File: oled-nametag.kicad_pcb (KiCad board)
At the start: 4 copper layers, 88 x 30 mm, 119 parts, among them J1 USB_C_Receptacle_USB2.0, J2 I2C, Q1 AO3401A, Q2 AO3401A, Q3 FS8205A, Q6 2N7002, SW1 Power, SW2 BTN1, SW3 BTN2, SW4 BTN3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

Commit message: Start rev1.1
Fixed bugs:
 - Swapped D+ and D-
 - Insufficient pull-down strength on VBUS
 - Default OLED to 4-wire SPI
 - Swap VBUS detect divider from 2/3 to 1/3
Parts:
- R21: value 47k -> 1k
- R28: value 5.1k -> 10k
- R30: value 10k -> 5.1k
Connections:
- R1 pad 1: +3V3 -> GND
- U3 pad 25: /ESP32/D+ -> /ESP32/D-
- U3 pad 26: /ESP32/D- -> /ESP32/D+
- U9 pad 4: /ESP32/D- -> /ESP32/D+
- U9 pad 6: /ESP32/D+ -> /ESP32/D-
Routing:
- net +3V3: track 67.1 -> 57.3 mm, vias 23 -> 22
- net GND: track 161.5 -> 163.5 mm
- net /ESP32/D-: track 52.1 -> 50.8 mm
- net /ESP32/D+: track 50.6 -> 51.2 mm
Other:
- board text added: "OLED Badge Rev 1.1 2023"
- board text removed: "OLED Badge Rev 1.0 2023"

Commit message: More Rev 1.1 fixes
- Revert USB_DET voltage divider swap
- Fix battery gauge temperature sensor reference level
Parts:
- R28: value 10k -> 5.1k
- R30: value 5.1k -> 10k
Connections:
- R33 pad 2: GND1 -> Net-(U10-VCC)
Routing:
- net Net-(U10-VCC): track 1.30 -> 5.02 mm, vias 0 -> 2
- net GND1: track 16.0 -> 15.4 mm, vias 20 -> 19
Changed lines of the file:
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@@
       (net 92 "Net-(U10-TS)") (pintype "passive"))
     (pad "2" smd roundrect (at 0.51 0) (size 0.54 0.64) (layers "F.Cu" "F.Paste" "F.Mask") (roundrect_rratio 0.25)
-      (net 16 "GND1") (pintype "passive"))
+      (net 17 "Net-(U10-VCC)") (pintype "passive"))
     (model "${KICAD6_3DMODEL_DIR}/Resistor_SMD.3dshapes/R_0402_1005Metric.wrl"
       (offset (xyz 0 0 0))
@@
     (descr "Resistor SMD 0402 (1005 Metric), square (rectangular) end terminal, IPC_7351 nominal, (Body size source: IPC-SM-782 page 72, https://www.pcb-3d.com/wordpress/wp-content/uploads/ipc-sm-782a_amendment_1_and_2.pdf), generated with kicad-footprint-generator")
     (tags "resistor")
-    (property "LCSC" "C25744")
+    (property "LCSC" "C25905")
     (property "Sheetfile" "power.kicad_sch")
     (property "Sheetname" "Power")
@@
         (effects (font (size 1 1) (thickness 0.15)))
     )
-    (fp_text value "10k" (at 0 1.17 90) (layer "F.Fab")
+    (fp_text value "5.1k" (at 0 1.17 90) (layer "F.Fab")
         (effects (font (size 1 1) (thickness 0.15)))
     )
@@
     (descr "Resistor SMD 0402 (1005 Metric), square (rectangular) end terminal, IPC_7351 nominal, (Body size source: IPC-SM-782 page 72, https://www.pcb-3d.com/wordpress/wp-content/uploads/ipc-sm-782a_amendment_1_and_2.pdf), generated with kicad-footprint-generator")
     (tags "resistor")
-    (property "LCSC" "C25905")
+    (property "LCSC" "C25744")
     (property "Sheetfile" "power.kicad_sch")
     (property "Sheetname" "Power")
@@
         (effects (font (size 1 1) (thickness 0.15)))
     )
-    (fp_text value "5.1k" (at 0 1.17 90) (layer "F.Fab")
+    (fp_text value "10k" (at 0 1.17 90) (layer "F.Fab")
         (effects (font (size 1 1) (thickness 0.15)))
     )
@@
   (segment (start 87.85 36.8) (end 87.5 36.8) (width 0.127) (layer "F.Cu") (net 16))
   (segment (start 90.100001 37.2) (end 90.1 36.3) (width 0.127) (layer "F.Cu") (net 16))
-  (segment (start 88.379999 38.9) (end 88.95 38.9) (width 0.127) (layer "F.Cu") (net 16))
   (segment (start 87.5 36.8) (end 87.35 36.8) (width 0.127) (layer "F.Cu") (net 16))
   (segment (start 89.15 37.25) (end 88.95 37.05) (width 0.127) (layer "F.Cu") (net 16))
@@
   (via (at 72.35 34.05) (size 0.45) (drill 0.3) (layers "F.Cu" "B.Cu") (net 16))
   (via (at 73.55 31.55) (size 0.45) (drill 0.3) (layers "F.Cu" "B.Cu") (net 16))
-  (via (at 88.95 38.9) (size 0.45) (drill 0.3) (layers "F.Cu" "B.Cu") (net 16))
   (via (at 105.75 38.75) (size 0.45) (drill 0.3) (layers "F.Cu" "B.Cu") (net 16))
   (via (at 22.25 38.65) (size 0.45) (drill 0.3) (layers "F.Cu" "B.Cu") (net 16))
@@
   (via (at 72.05 31.55) (size 0.45) (drill 0.3) (layers "F.Cu" "B.Cu") (net 16))
   (via (at 72.8 31.55) (size 0.45) (drill 0.3) (layers "F.Cu" "B.Cu") (net 16))
-  (segment (start 89.15 36.3) (end 87.85 36.3) (width 0.127) (layer "F.Cu") (net 17))
+  (segment (start 89.15 36.3) (end 88.55 36.3) (width 0.127) (layer "F.Cu") (net 17))
+  (segment (start 88.379999 38.9) (end 88.95 38.9) (width 0.127) (layer "F.Cu") (net 17))
+  (segment (start 88.55 36.3) (end 88.55 36.15) (width 0.127) (layer "F.Cu") (net 17))
+  (segment (start 88.55 36.3) (end 87.85 36.3) (width 0.127) (layer "F.Cu") (net 17))
+  (via (at 88.55 36.15) (size 0.45) (drill 0.2) (layers "F.Cu" "B.Cu") (net 17))
+  (via (at 88.95 38.9) (size 0.45) (drill 0.2) (layers "F.Cu" "B.Cu") (net 17))
+  (segment (start 89.05 38.8) (end 88.95 38.9) (width 0.127) (layer "B.Cu") (net 17))
+  (segment (start 89.05 36.65) (end 89.05 38.8) (width 0.127) (layer "B.Cu") (net 17))
+  (segment (start 88.55 36.15) (end 89.05 36.65) (width 0.127) (layer "B.Cu") (net 17))
   (segment (start 86.320002 34.7) (end 87.12 34.7) (width 0.127) (layer "F.Cu") (net 18))
   (segment (start 87.349999 35.8) (end 87.35 34.7) (width 0.127) (layer "F.Cu") (net 18))

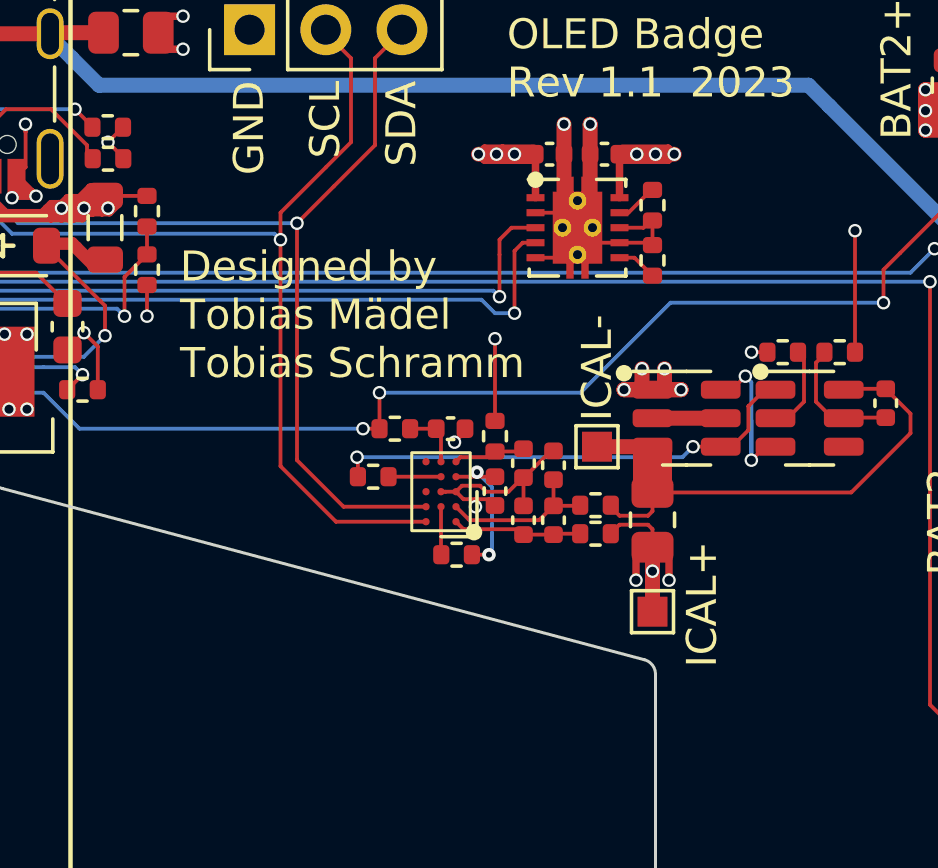
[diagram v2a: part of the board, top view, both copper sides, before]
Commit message: Reduce charge current to 300mA, Add battery voltage calibration testpoint
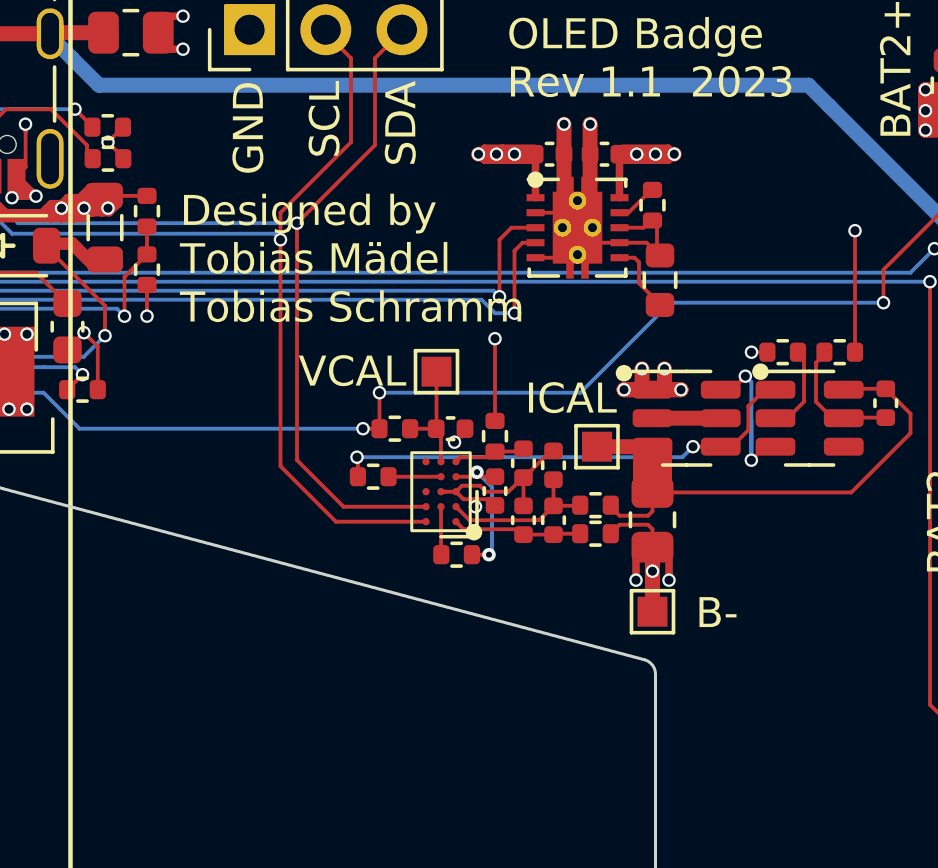
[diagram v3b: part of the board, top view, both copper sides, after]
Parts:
- added TP10: VCAL, TestPoint:TestPoint_Pad_1.0x1.0mm, F.Cu at (87.2, 32.8)
- R14: value 1k -> 2.7k; footprint Resistor_SMD:R_0402_1005Metric -> Resistor_SMD:R_0603_1608Metric
- moved R14 0.71 mm to (94.7, 29.8)
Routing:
- net Net-(U10-BAT): track 1.90 -> 3.80 mm
- net Net-(U8-ISET): track 1.35 -> 2.40 mm
- net GND: track 163.5 -> 164.4 mm
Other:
- board text added: "B-"
- board text added: "ICAL"
- board text added: "VCAL"
- board text removed: "ICAL+"
- board text removed: "ICAL-"

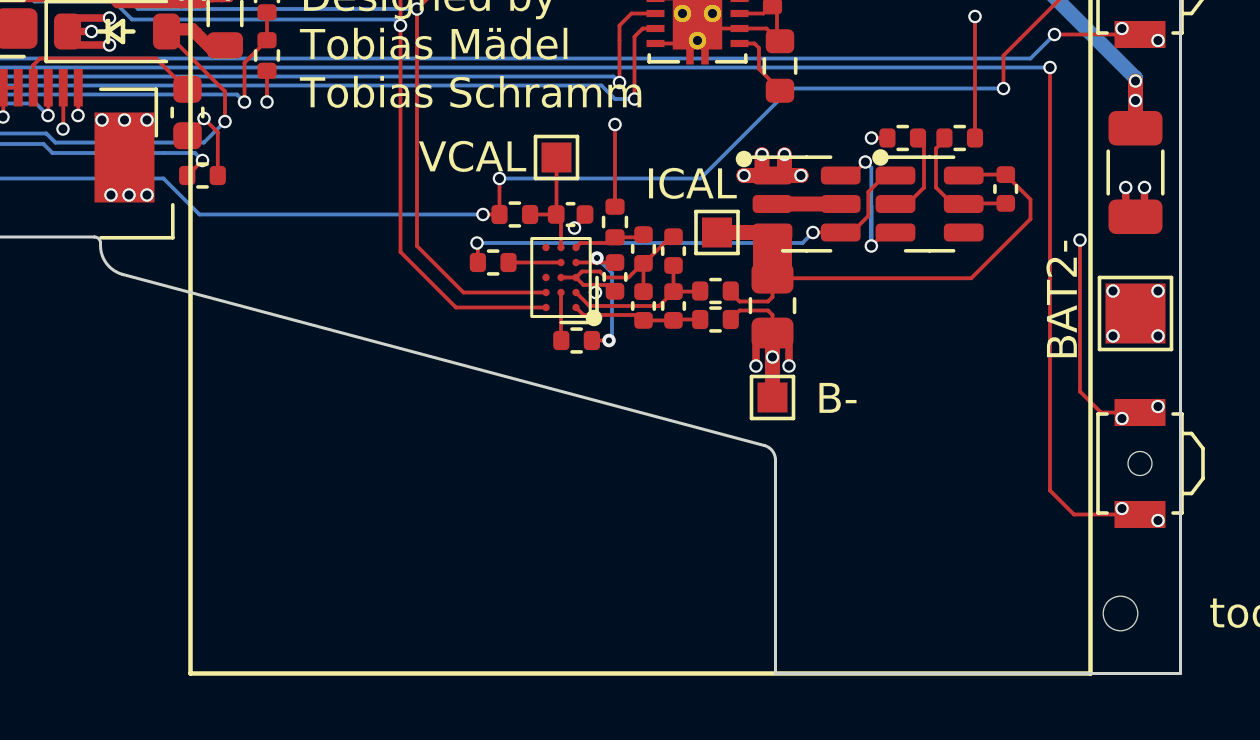
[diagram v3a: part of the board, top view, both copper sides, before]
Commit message: Add current calibration output
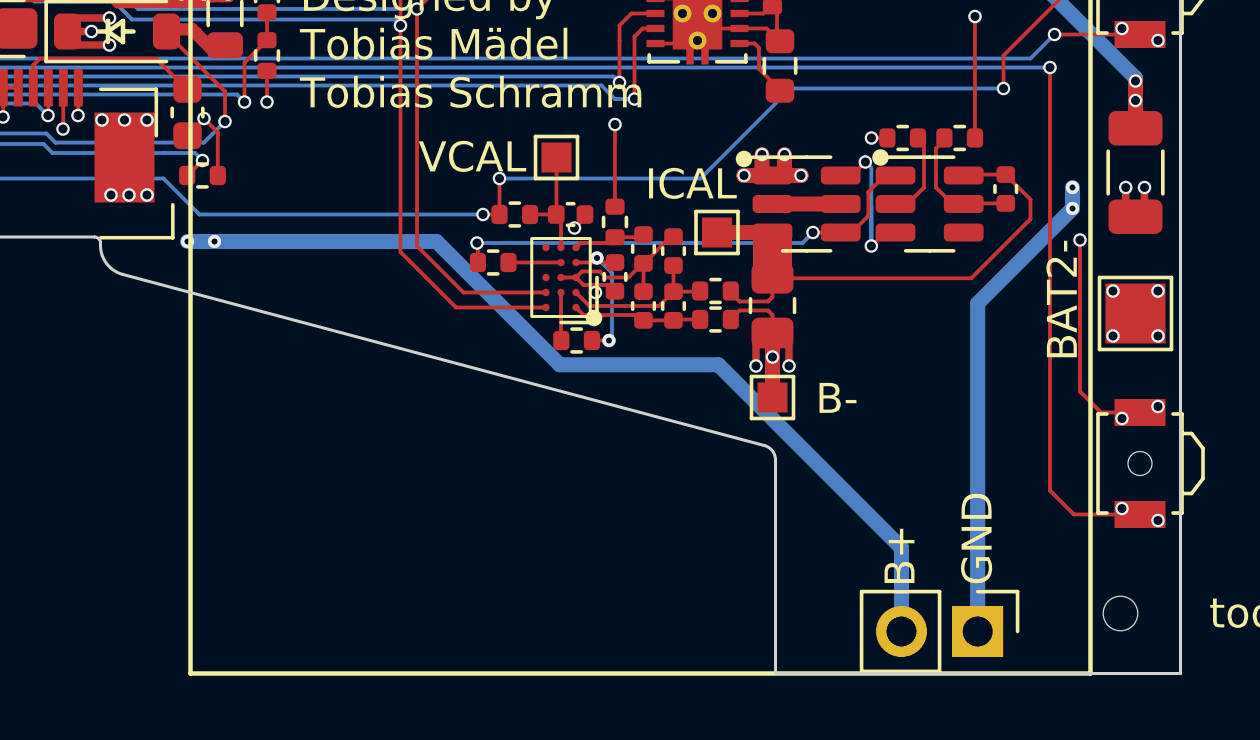
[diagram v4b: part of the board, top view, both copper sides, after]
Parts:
- added J3: LOAD, Connector_PinHeader_2.54mm:PinHeader_1x02_P2.54mm_Vertical, F.Cu at (101.2, 48.6)
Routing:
- net +BATT: track 129.4 -> 160.2 mm, vias 22 -> 24
- net GND: track 164.4 -> 180.5 mm, vias 90 -> 92
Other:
- board text added: "B+"
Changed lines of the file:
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@@
     )
   )
+  (footprint "Connector_PinHeader_2.54mm:PinHeader_1x02_P2.54mm_Vertical" (layer "F.Cu")
+    (at 101.24 48.6 -90)
+    (descr "Through hole straight pin header, 1x02, 2.54mm pitch, single row")
+    (tags "Through hole pin header THT 1x02 2.54mm single row")
+    (property "Sheetfile" "power.kicad_sch")
+    (property "Sheetname" "Power")
+    (property "ki_description" "Generic connector, single row, 01x02, script generated (kicad-library-utils/schlib/autogen/connector/)")
+    (property "ki_keywords" "connector")
+    (attr through_hole)
+    (fp_text reference "J3" (at 0 -2.33 90) (layer "F.SilkS") hide
+        (effects (font (size 1 1) (thickness 0.15)))
+    )
+    (fp_text value "LOAD" (at 0 4.87 90) (layer "F.Fab")
+        (effects (font (size 1 1) (thickness 0.15)))
+    )
+    (fp_text user "${REFERENCE}" (at 0 1.27) (layer "F.Fab")
+        (effects (font (size 1 1) (thickness 0.15)))
+    )
+    (fp_line (start -1.33 -1.33) (end 0 -1.33)
+      (stroke (width 0.12) (type solid)) (layer "F.SilkS"))
+    (fp_line (start -1.33 0) (end -1.33 -1.33)
+      (stroke (width 0.12) (type solid)) (layer "F.SilkS"))
+    (fp_line (start -1.33 1.27) (end -1.33 3.87)
+      (stroke (width 0.12) (type solid)) (layer "F.SilkS"))
+    (fp_line (start -1.33 1.27) (end 1.33 1.27)
+      (stroke (width 0.12) (type solid)) (layer "F.SilkS"))
+    (fp_line (start -1.33 3.87) (end 1.33 3.87)
+      (stroke (width 0.12) (type solid)) (layer "F.SilkS"))
+    (fp_line (start 1.33 1.27) (end 1.33 3.87)
+      (stroke (width 0.12) (type solid)) (layer "F.SilkS"))
+    (fp_line (start -1.8 -1.8) (end -1.8 4.35)
+      (stroke (width 0.05) (type solid)) (layer "F.CrtYd"))
+    (fp_line (start -1.8 4.35) (end 1.8 4.35)
+      (stroke (width 0.05) (type solid)) (layer "F.CrtYd"))
+    (fp_line (start 1.8 -1.8) (end -1.8 -1.8)
+      (stroke (width 0.05) (type solid)) (layer "F.CrtYd"))
+    (fp_line (start 1.8 4.35) (end 1.8 -1.8)
+      (stroke (width 0.05) (type solid)) (layer "F.CrtYd"))
+    (fp_line (start -1.27 -0.635) (end -0.635 -1.27)
+      (stroke (width 0.1) (type solid)) (layer "F.Fab"))
+    (fp_line (start -1.27 3.81) (end -1.27 -0.635)
+      (stroke (width 0.1) (type solid)) (layer "F.Fab"))
+    (fp_line (start -0.635 -1.27) (end 1.27 -1.27)
+      (stroke (width 0.1) (type solid)) (layer "F.Fab"))
+    (fp_line (start 1.27 -1.27) (end 1.27 3.81)
+      (stroke (width 0.1) (type solid)) (layer "F.Fab"))
+    (fp_line (start 1.27 3.81) (end -1.27 3.81)
+      (stroke (width 0.1) (type solid)) (layer "F.Fab"))
+    (pad "1" thru_hole rect (at 0 0 270) (size 1.7 1.7) (drill 1) (layers "*.Cu" "*.Mask")
+      (net 6 "GND") (pinfunction "Pin_1") (pintype "passive"))
+    (pad "2" thru_hole oval (at 0 2.54 270) (size 1.7 1.7) (drill 1) (layers "*.Cu" "*.Mask")
+      (net 15 "+BATT") (pinfunction "Pin_2") (pintype "passive"))
+  )
   (footprint "Resistor_SMD:R_0402_1005Metric" (layer "F.Cu")
     (at 44.69 27.2)
@@
   (gr_rect (start 23 20) (end 53 50)
     (stroke (width 0.15) (type solid)) (fill none) (layer "User.9"))
+  (gr_text "GND" (at 101.24 47.07 90) (layer "F.SilkS")
+    (effects (font (size 1 1) (thickness 0.15)) (justify left))
+  )
   (gr_text "GND" (at 24.55 25.4 90) (layer "F.SilkS")
     (effects (font (size 1 1) (thickness 0.15)) (justify left))
@@
     (effects (font (size 1 1) (thickness 0.15)) (justify top))
   )
+  (gr_text "B+" (at 98.67 47.12 90) (layer "F.SilkS")
+    (effects (font (size 1 1) (thickness 0.15)) (justify left))
+  )
   (gr_text "BAT2-" (at 103.5 37.55 90) (layer "F.SilkS")
     (effects (font (size 1 1) (thickness 0.15)) (justify top))
@@
   (via (at 106.175 33.8) (size 0.45) (drill 0.3) (layers "F.Cu" "B.Cu") (net 6))
   (via (at 24.55 27.65) (size 0.45) (drill 0.3) (layers "F.Cu" "B.Cu") (net 6))
+  (via (at 104.4 34.5) (size 0.45) (drill 0.2) (layers "F.Cu" "B.Cu") (net 6))
   (via (at 51.85 31.15) (size 0.45) (drill 0.3) (layers "F.Cu" "B.Cu") (net 6))
   (via (at 106.05 41.5) (size 0.45) (drill 0.3) (layers "F.Cu" "B.Cu") (net 6))
@@
   (via (at 55.25 31.55) (size 0.45) (drill 0.3) (layers "F.Cu" "B.Cu") (net 6))
   (via (at 55.340623 22.701565) (size 0.45) (drill 0.3) (layers "F.Cu" "B.Cu") (net 6))
+  (via (at 104.4 33.8) (size 0.45) (drill 0.2) (layers "F.Cu" "B.Cu") (net 6))
   (via (at 92.325 24.55) (size 0.45) (drill 0.3) (layers "F.Cu" "B.Cu") (net 6))
   (via (at 68.75 31.45) (size 0.45) (drill 0.3) (layers "F.Cu" "B.Cu") (net 6))
@@
   (via (at 49.4 29.75) (size 0.45) (drill 0.3) (layers "F.Cu" "B.Cu") (net 6))
   (via (at 106.05 25.5) (size 0.45) (drill 0.3) (layers "F.Cu" "B.Cu") (net 6))
+  (segment (start 101.24 48.6) (end 101.24 37.66) (width 0.5) (layer "B.Cu") (net 6))
+  (segment (start 104.4 34.5) (end 104.4 33.8) (width 0.5) (layer "B.Cu") (net 6))
+  (segment (start 101.24 37.66) (end 104.4 34.5) (width 0.5) (layer "B.Cu") (net 6))
   (segment (start 69.983 29.5) (end 73.85 29.5) (width 0.127) (layer "F.Cu") (net 7))
   (segment (start 69.76 30.475) (end 69.76 29.723) (width 0.127) (layer "F.Cu") (net 7))
@@
   (via (at 95.125 25.55) (size 0.45) (drill 0.3) (layers "F.Cu" "B.Cu") (net 15))
   (via (at 46.8 31.15) (size 0.45) (drill 0.3) (layers "F.Cu" "B.Cu") (net 15))
+  (via (at 74.9 35.6) (size 0.45) (drill 0.2) (layers "F.Cu" "B.Cu") (net 15))
   (via (at 85.3 33.5) (size 0.45) (drill 0.3) (layers "F.Cu" "B.Cu") (net 15))
   (via (at 45.85 31.15) (size 0.45) (drill 0.3) (layers "F.Cu" "B.Cu") (net 15))
@@
   (via (at 23.75 46.85) (size 0.45) (drill 0.3) (layers "F.Cu" "B.Cu") (net 15))
   (via (at 104.25 23.4) (size 0.45) (drill 0.3) (layers "F.Cu" "B.Cu") (net 15))
+  (via (at 75.8 35.6) (size 0.45) (drill 0.2) (layers "F.Cu" "B.Cu") (net 15))
   (via (at 93.875 25.55) (size 0.45) (drill 0.3) (layers "F.Cu" "B.Cu") (net 15))
   (via (at 22.95 46.15) (size 0.45) (drill 0.3) (layers "F.Cu" "B.Cu") (net 15))
+  (segment (start 87.31 39.71) (end 83.2 35.6) (width 0.5) (layer "B.Cu") (net 15))
   (segment (start 66.1 33.85) (end 66.45 33.5) (width 0.127) (layer "B.Cu") (net 15))
   (segment (start 95 30.5) (end 92 33.5) (width 0.127) (layer "B.Cu") (net 15))
@@
   (segment (start 102.1 30.5) (end 95 30.5) (width 0.127) (layer "B.Cu") (net 15))
   (segment (start 24.151883 41.648117) (end 24.15 41.65) (width 0.127) (layer "B.Cu") (net 15))
+  (segment (start 92.597736 39.71) (end 87.31 39.71) (width 0.5) (layer "B.Cu") (net 15))
   (segment (start 92 33.5) (end 85.3 33.5) (width 0.127) (layer "B.Cu") (net 15))
   (segment (start 53.25 34.6) (end 54 33.85) (width 0.127) (layer "B.Cu") (net 15))
+  (segment (start 98.7 45.812264) (end 92.597736 39.71) (width 0.5) (layer "B.Cu") (net 15))
   (segment (start 52.1 36.85) (end 53.25 35.7) (width 0.127) (layer "B.Cu") (net 15))
   (segment (start 33.307373 41.648117) (end 24.151883 41.648117) (width 0.127) (layer "B.Cu") (net 15))
   (segment (start 53.25 35.7) (end 53.25 35.6) (width 0.127) (layer "B.Cu") (net 15))
+  (segment (start 98.7 48.6) (end 98.7 45.812264) (width 0.5) (layer "B.Cu") (net 15))
   (segment (start 75.3 34.7) (end 84.75 34.7) (width 0.127) (layer "B.Cu") (net 15))
+  (segment (start 83.2 35.6) (end 75.8 35.6) (width 0.5) (layer "B.Cu") (net 15))
   (segment (start 42.707373 39.248117) (end 52.1 36.85) (width 0.127) (layer "B.Cu") (net 15))
   (segment (start 66.45 33.5) (end 74.1 33.5) (width 0.127) (layer "B.Cu") (net 15))
   (segment (start 74.1 33.5) (end 75.3 34.7) (width 0.127) (layer "B.Cu") (net 15))
   (segment (start 33.307373 41.648117) (end 42.7 39.25) (width 0.127) (layer "B.Cu") (net 15))
+  (segment (start 75.8 35.6) (end 74.9 35.6) (width 0.5) (layer "B.Cu") (net 15))
   (segment (start 88.5 37.05) (end 88.1 37.05) (width 0.127) (layer "F.Cu") (net 16))
   (segment (start 94.15 38.65) (end 93.85 38.95) (width 0.25) (layer "F.Cu") (net 16))
